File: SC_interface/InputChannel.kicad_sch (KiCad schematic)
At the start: 44 parts, among them J4 Input2, J5 BalancedOut2, J6 Output_BNC12, Q5 LND150N8, Q6 LND150N8, Q7 LND150N8, Q8 LND150N8, SW3 SW_Select2, U5 DRV135UA, U6 U2 OPA1656IDR, U7 INA134UA

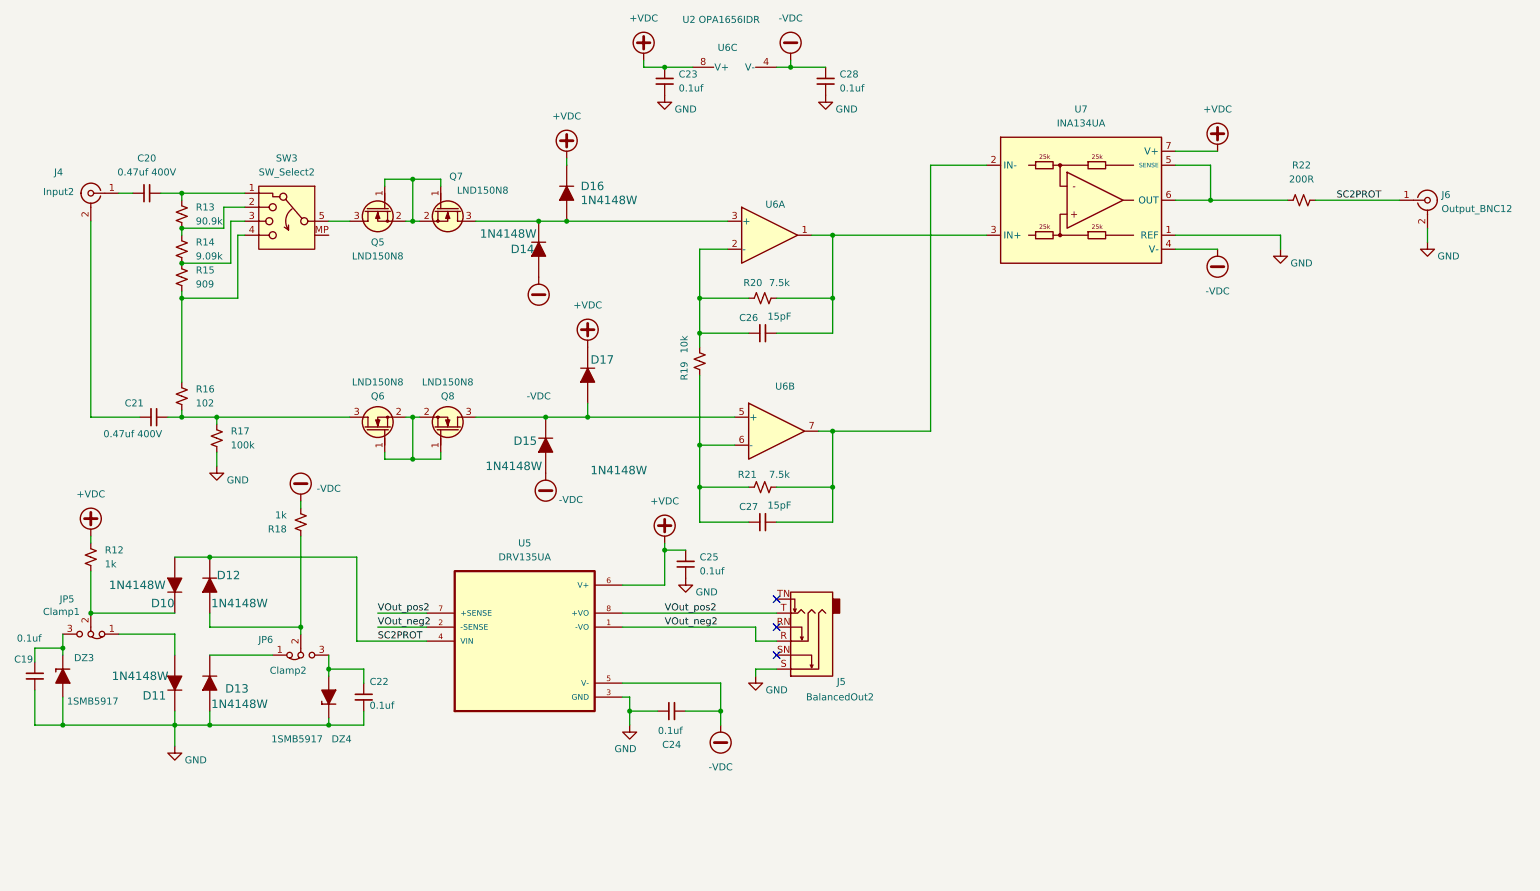
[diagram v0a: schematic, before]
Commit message: schemetic change and initial 3D rendering
Added master switch, some LED, Test Point.
Fixed all the footprint issues, passed ECE check
Initial 3D rendering the PCB update
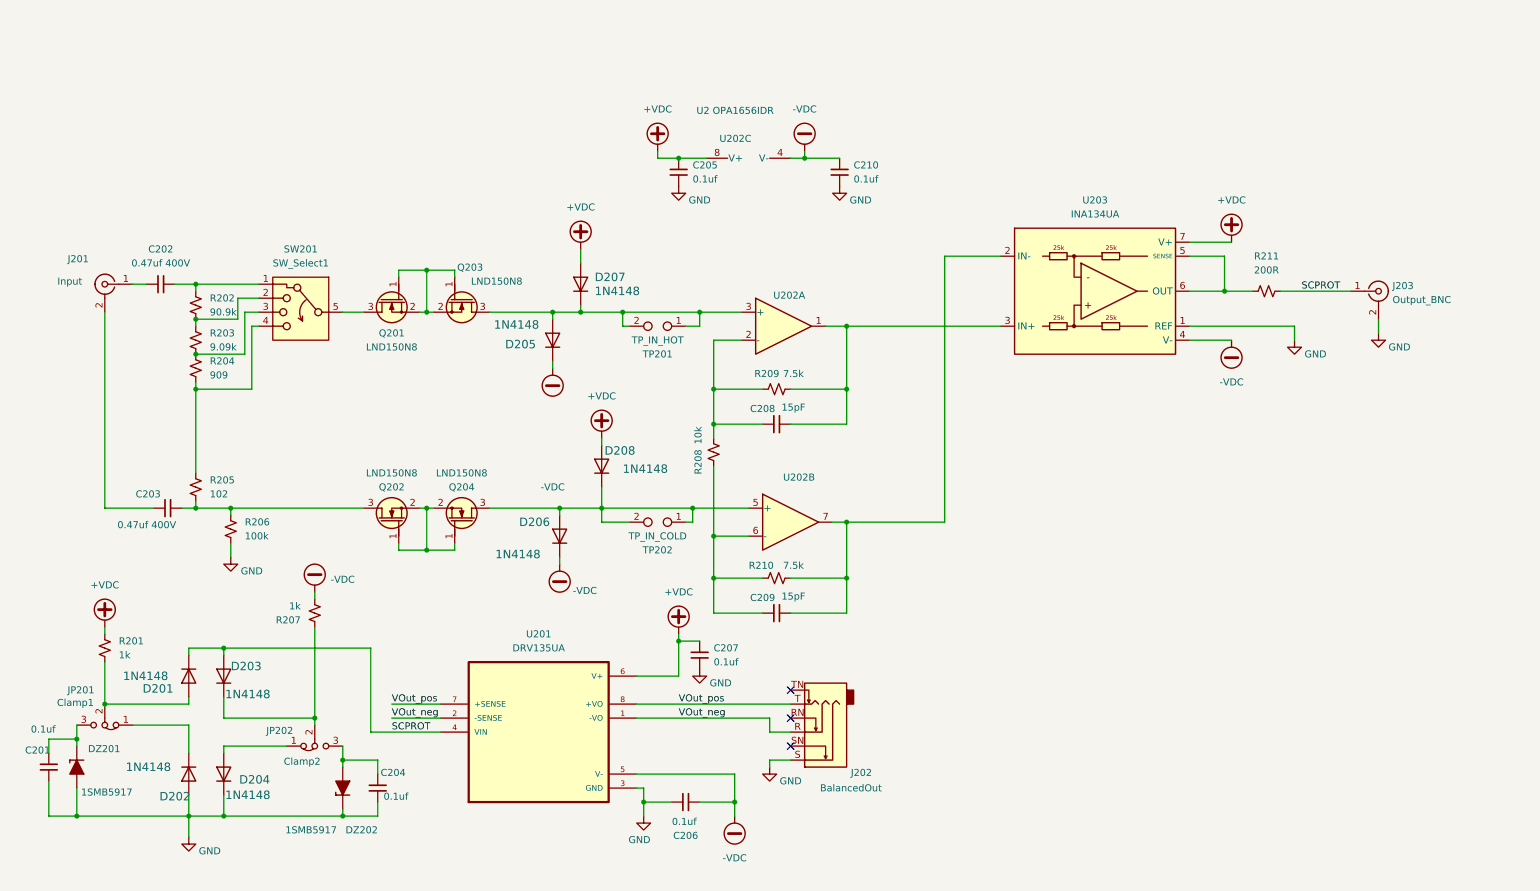
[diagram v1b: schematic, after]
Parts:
- removed C19, C22, C23, C24, C25, C28: 0.1uf, symbol Device:C_Small
- removed C20, C21: 0.47uf 400V, symbol Device:C_Small
- removed C26, C27: 15pF, PCM_SparkFun-Resistor:R_0603_1608Metric, symbol Device:C_Small
- removed D10, D11, D12, D13, D14, D15, D16, D17: 1N4148W, digikey-footprints:SOD-123, symbol dk_Diodes-Rectifiers-Single:1N4148W-7-F
- removed DZ3, DZ4: 1SMB5917, PCM_Diode_SMD_AKL:D_SMB, symbol PCM_Diode_Zener_AKL:1SMB5917
- removed J4: Input2, PCM_SparkFun-Connector:1x02, symbol Connector:Conn_Coaxial
- removed J5: BalancedOut2, Connector_Audio:Jack_6.35mm_Neutrik_NMJ6HCD2_Horizontal, symbol Connector_Audio:NMJ6HCD2
- removed J6: Output_BNC12, PCM_SparkFun-Connector:1x02, symbol Connector:Conn_Coaxial
- removed JP5: Clamp1, Package_LCC:PLCC-84_29.3x29.3mm_P1.27mm, symbol Jumper:Jumper_3_Bridged12
- removed JP6: Clamp2, Package_LCC:PLCC-84_29.3x29.3mm_P1.27mm, symbol Jumper:Jumper_3_Bridged12
- removed Q5, Q6, Q7, Q8: LND150N8, PCM_Package_TO_SOT_SMD_AKL:SOT-89-3, symbol PCM_Transistor_MOSFET_AKL:LND150N8
- removed R12, R18: 1k, PCM_SparkFun-Resistor:R_0603_1608Metric, symbol PCM_SparkFun-Resistor:R_Small
- removed R13: 90.9k, PCM_SparkFun-Resistor:R_0603_1608Metric, symbol PCM_SparkFun-Resistor:R_Small
- removed R14: 9.09k, PCM_SparkFun-Resistor:R_0603_1608Metric, symbol PCM_SparkFun-Resistor:R_Small
- removed R15: 909, PCM_SparkFun-Resistor:R_0603_1608Metric, symbol PCM_SparkFun-Resistor:R_Small
- removed R16: 102, PCM_SparkFun-Resistor:R_0603_1608Metric, symbol PCM_SparkFun-Resistor:R_Small
- removed R17: 100k, PCM_SparkFun-Resistor:R_0603_1608Metric, symbol PCM_SparkFun-Resistor:R_Small
- removed R19: 10k, PCM_SparkFun-Resistor:R_0603_1608Metric, symbol PCM_SparkFun-Resistor:R_Small
- removed R20, R21: 7.5k, PCM_SparkFun-Resistor:R_0603_1608Metric, symbol PCM_SparkFun-Resistor:R_Small
- removed R22: 200R, PCM_SparkFun-Resistor:R_0603_1608Metric, symbol PCM_SparkFun-Resistor:R_Small
- removed SW3: SW_Select2, PCM_SparkFun-Resistor:R_0603_1608Metric, symbol Switch:SW_Rotary_1x4_MP
- removed U5: DRV135UA, DRV135UA:SOIC127P599X175-8N, symbol DRV135UA:DRV135UA
- removed U6: U2 OPA1656IDR, Package_SO:SOIC-8_3.9x4.9mm_P1.27mm, symbol Amplifier_Operational:OPA1656ID
- removed U7: INA134UA, PCM_Package_SO_AKL:SO-8_3.9x4.9mm_P1.27mm, symbol PCM_Amplifier_Difference_AKL:INA134UA
- added C201, C204, C205, C206, C207, C210: 0.1uf, Capacitor_SMD:C_0805_2012Metric_Pad1.18x1.45mm_HandSolder, symbol Device:C_Small
- added C202, C203: 0.47uf 400V, Capacitor_THT:C_Rect_L13.0mm_W4.0mm_P10.00mm_FKS3_FKP3_MKS4, symbol Device:C_Small
- added C208, C209: 15pF, Capacitor_SMD:C_0805_2012Metric_Pad1.18x1.45mm_HandSolder, symbol Device:C_Small
- added D201, D202, D203, D204, D205, D206, D207, D208: 1N4148, Diode_THT:D_DO-35_SOD27_P7.62mm_Horizontal, symbol Diode:1N4148
- added DZ201, DZ202: 1SMB5917, Diode_SMD:D_SMB-SMC_Universal_Handsoldering, symbol PCM_Diode_Zener_AKL:1SMB5917
- added J201: Input, Connector_PinHeader_2.54mm:PinHeader_1x02_P2.54mm_Vertical, symbol Connector:Conn_Coaxial
- added J202: BalancedOut, Connector_Audio:Jack_6.35mm_Neutrik_NMJ6HCD2_Horizontal, symbol Connector_Audio:NMJ6HCD2
- added J203: Output_BNC, Connector_PinHeader_2.54mm:PinHeader_1x02_P2.54mm_Vertical, symbol Connector:Conn_Coaxial
- added JP201: Clamp1, Connector_PinHeader_2.54mm:PinHeader_1x03_P2.54mm_Vertical, symbol Jumper:Jumper_3_Bridged12
- added JP202: Clamp2, Connector_PinHeader_2.54mm:PinHeader_1x03_P2.54mm_Vertical, symbol Jumper:Jumper_3_Bridged12
- added Q201, Q202, Q203, Q204: LND150N8, Package_TO_SOT_SMD:SOT-89-3_Handsoldering, symbol PCM_Transistor_MOSFET_AKL:LND150N8
- added R201, R207: 1k, Resistor_SMD:R_0805_2012Metric_Pad1.20x1.40mm_HandSolder, symbol PCM_SparkFun-Resistor:R_Small
- added R202: 90.9k, Resistor_SMD:R_MELF_MMB-0207, symbol PCM_SparkFun-Resistor:R_Small
- added R203: 9.09k, Resistor_SMD:R_1206_3216Metric_Pad1.30x1.75mm_HandSolder, symbol PCM_SparkFun-Resistor:R_Small
- added R204: 909, Resistor_SMD:R_0805_2012Metric_Pad1.20x1.40mm_HandSolder, symbol PCM_SparkFun-Resistor:R_Small
- added R205: 102, Resistor_SMD:R_0805_2012Metric_Pad1.20x1.40mm_HandSolder, symbol PCM_SparkFun-Resistor:R_Small
- added R206: 100k, Resistor_SMD:R_0805_2012Metric_Pad1.20x1.40mm_HandSolder, symbol PCM_SparkFun-Resistor:R_Small
- added R208: 10k, Resistor_SMD:R_0805_2012Metric_Pad1.20x1.40mm_HandSolder, symbol PCM_SparkFun-Resistor:R_Small
- added R209, R210: 7.5k, Resistor_SMD:R_0805_2012Metric_Pad1.20x1.40mm_HandSolder, symbol PCM_SparkFun-Resistor:R_Small
- added R211: 200R, Resistor_SMD:R_0805_2012Metric_Pad1.20x1.40mm_HandSolder, symbol PCM_SparkFun-Resistor:R_Small
- added SW201: SW_Select1, Connector_PinHeader_2.54mm:PinHeader_1x05_P2.54mm_Vertical, symbol Switch:SW_Rotary_1x4_MP
- added TP201: TP_IN_HOT, Connector_PinHeader_2.54mm:PinHeader_1x02_P2.54mm_Vertical, symbol Connector:TestPoint_2Pole
- added TP202: TP_IN_COLD, Connector_PinHeader_2.54mm:PinHeader_1x02_P2.54mm_Vertical, symbol Connector:TestPoint_2Pole
- added U201: DRV135UA, Package_SO:SOIC-8_3.9x4.9mm_P1.27mm, symbol DRV135UA:DRV135UA
- added U202: U2 OPA1656IDR, Package_SO:SOIC-8_3.9x4.9mm_P1.27mm, symbol Amplifier_Operational:OPA1656ID
- added U203: INA134UA, Package_SO:SOIC-8_3.9x4.9mm_P1.27mm, symbol PCM_Amplifier_Difference_AKL:INA134UA
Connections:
- net +VDC: now also C205.1, C207.1, D207.2 (A), D208.2 (A), R201.2, U201.6 (V+), U202.8 (V+), U203.7 (V+)
- net -VDC: now also C206.2, C210.1, D205.1 (K), D206.1 (K), R207.1, U201.5 (V-), U202.4 (V-), U203.4 (V-)
- net GND: now also C201.1, C204.1, C205.2, C206.1, C207.2, C210.2, D202.2 (A), D204.1 (K), DZ201.2 (A), DZ202.1 (K), J202.S, J203.2 (Ext), R206.1, U201.3 (GND), U203.1 (REF)
- new net: D201.2 (A), JP201.2 (C), R201.1
- new net: D204.2 (A), JP202.1 (A)
- new net: C202.1, J201.1 (In)
- new net: C202.2, R202.2, SW201.1
- new net: D203.1 (K), JP202.2 (C), R207.2
- new net: C204.2, DZ202.2 (A), JP202.3 (B)
- new net: C203.1, J201.2 (Ext)
- new net: C203.2, Q202.3 (D), R205.1, R206.2
- new net: R211.1, U203.5 (SENSE), U203.6 (OUT)
- new net: Q201.1 (G), Q201.2 (S), Q203.1 (G), Q203.2 (S)
- new net: D205.2 (A), D207.1 (K), Q203.3 (D), TP201.1, TP201.2, U202.3 (+)
- new net: D206.2 (A), D208.1 (K), Q204.3 (D), TP202.1, TP202.2, U202.5 (+)
- new net: R204.1, R205.2, SW201.4
- new net: R203.1, R204.2, SW201.3
- new net: R202.1, R203.2, SW201.2
- new net: C201.2, DZ201.1 (K), JP201.3 (B)
- new net: Q201.3 (D), SW201.5
- new net: D202.1 (K), JP201.1 (A)
- new net: C209.1, R208.1, R210.1, U202.6 (-)
- new net: C209.2, R210.2, U202.7, U203.2 (IN-)
- new net: Q202.1 (G), Q202.2 (S), Q204.1 (G), Q204.2 (S)
- new net: C208.2, R209.2, U202.1, U203.3 (IN+)
- new net: C208.1, R208.2, R209.1, U202.2 (-)
- new net SCPROT: D201.1 (K), D203.2 (A), J203.1 (In), R211.2, U201.4 (VIN)
- new net VOut_neg: J202.R, U201.1 (-VO), U201.2 (-SENSE)
- new net VOut_pos: J202.T, U201.7 (+SENSE), U201.8 (+VO)

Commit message: schematic changes
1. added TVS at output of DC-DC convert to prevent kick back
2. Changed all diodes to BAV199
3. change the Cfeedback to 4.7uF
4. removed LND Fet, replaced it with 4.7 K ohm
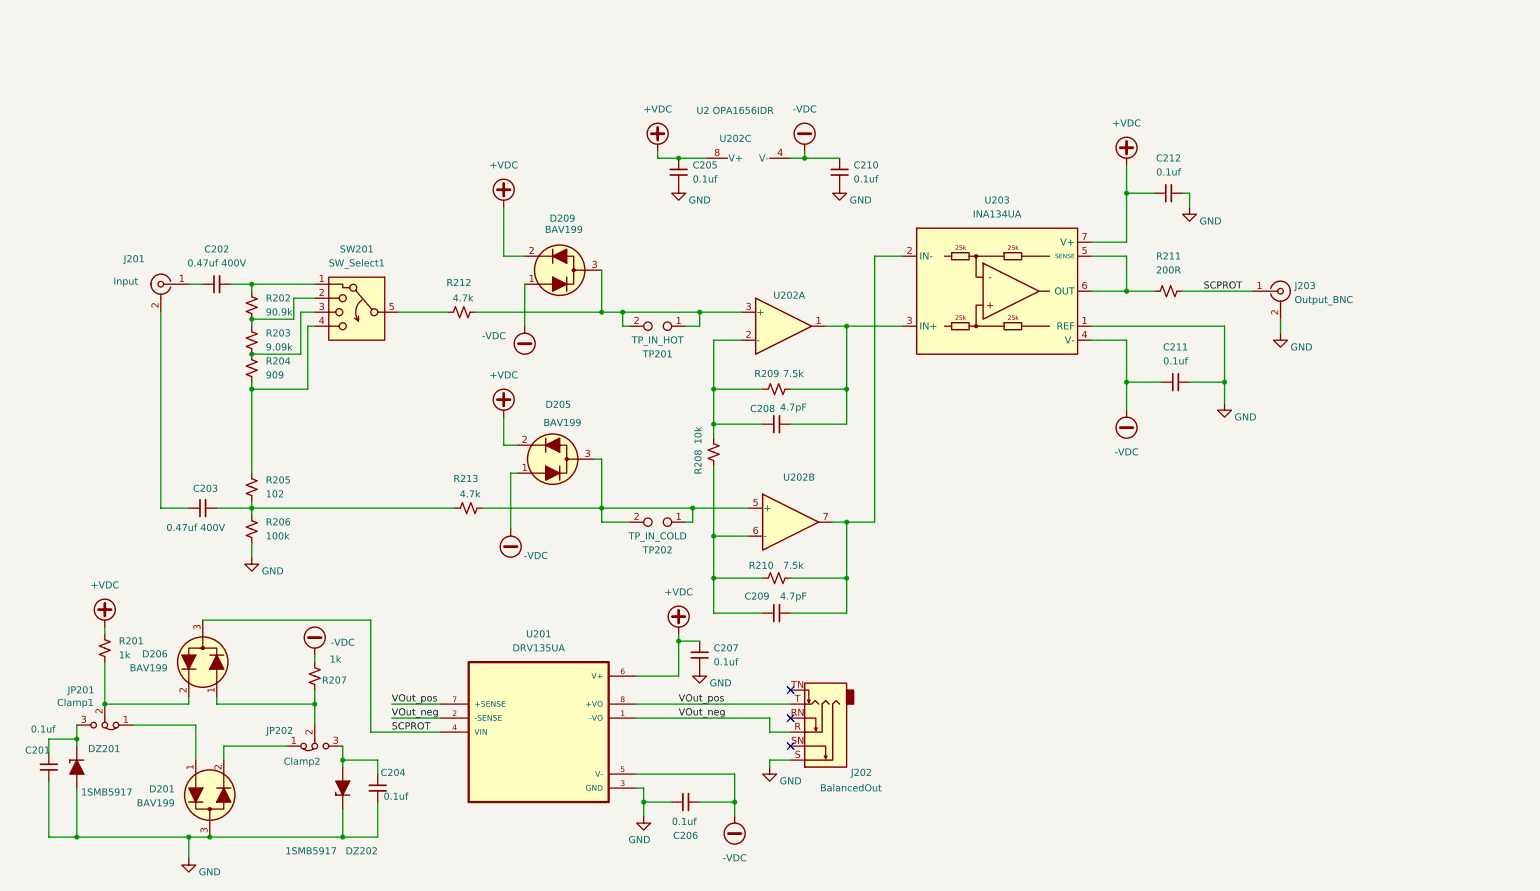
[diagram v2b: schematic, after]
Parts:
- removed D201, D202, D203, D204, D205, D206, D207, D208: 1N4148, Diode_THT:D_DO-35_SOD27_P7.62mm_Horizontal, symbol Diode:1N4148
- removed Q201, Q202, Q203, Q204: LND150N8, Package_TO_SOT_SMD:SOT-89-3_Handsoldering, symbol PCM_Transistor_MOSFET_AKL:LND150N8
- added C211, C212: 0.1uf, Capacitor_SMD:C_0805_2012Metric_Pad1.18x1.45mm_HandSolder, symbol Device:C_Small
- added D201, D205, D206, D209: BAV199, PCM_Package_TO_SOT_SMD_AKL:SOT-23, symbol PCM_Diode_AKL:BAV199
- added R212, R213: 4.7k, Resistor_THT:R_Axial_DIN0207_L6.3mm_D2.5mm_P15.24mm_Horizontal, symbol PCM_SparkFun-Resistor:R_Small
- C208, C209: value 15pF -> 4.7pF
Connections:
- net +VDC: now also C212.1, D205.2 (K), D209.2 (K)
- net -VDC: now also C211.1, D205.1 (A), D209.1 (A)
- net GND: now also C211.2, C212.2, D201.3 (C)
- net SCPROT: now also D206.3 (C)
- net at JP201.2 (C), R201.1: now also D206.2 (K)
- net at JP202.1 (A): now also D201.2 (K)
- net at JP202.2 (C), R207.2: now also D206.1 (A)
- net at C203.2, R205.1, R206.2: now also R213.1
- net at TP201.1, TP201.2, U202.3 (+): now also D209.3 (C), R212.2
- net at TP202.1, TP202.2, U202.5 (+): now also D205.3 (C), R213.2
- net at SW201.5: now also R212.1
- net at JP201.1 (A): now also D201.1 (A)
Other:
- moved on the sheet: C202, C203, J201, J203, R202, R203, R204, R205, R206, R207, R211, SW201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
